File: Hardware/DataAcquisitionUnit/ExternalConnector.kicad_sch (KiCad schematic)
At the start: 3 parts, among them J1 DE9_Pins_MountingHoles, J2 Conn_Coaxial, J3 Conn_Coaxial

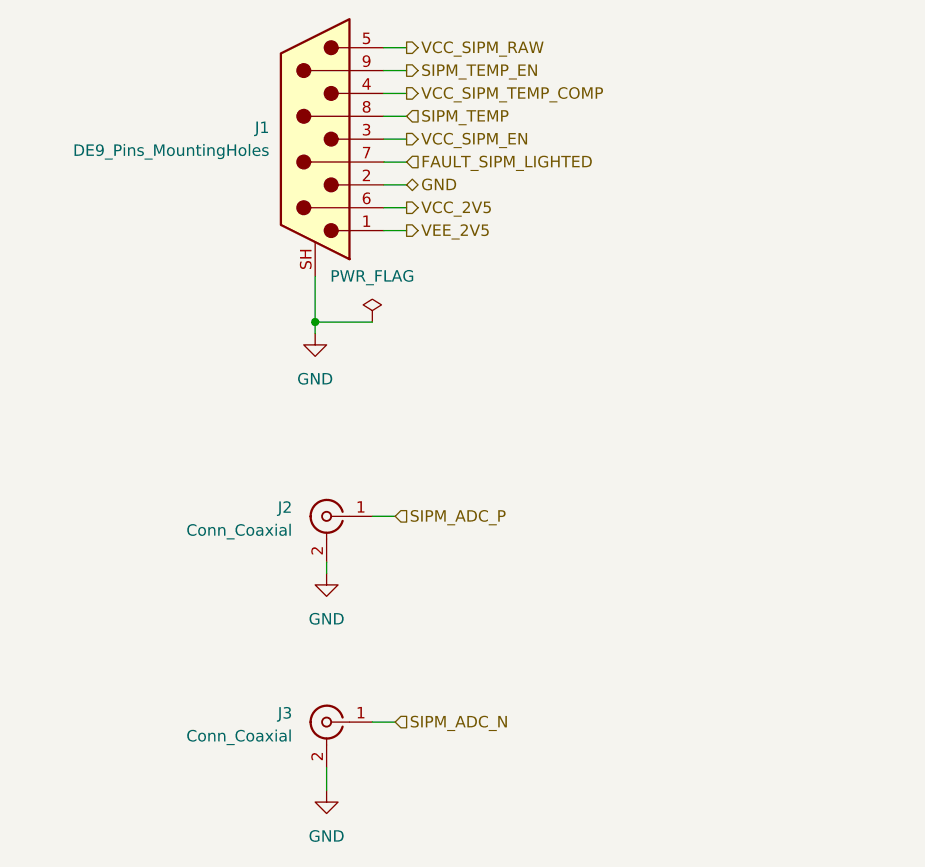
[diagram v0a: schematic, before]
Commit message: fix: #129, fix: #127
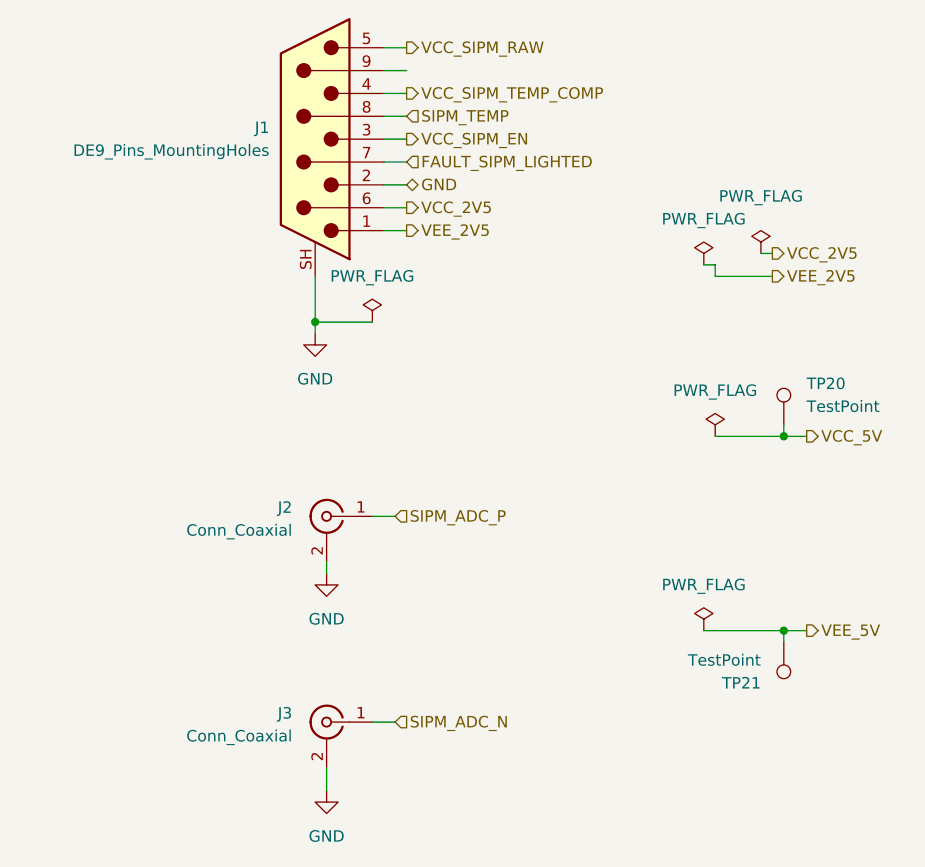
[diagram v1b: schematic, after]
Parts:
- added TP20, TP21: TestPoint, TestPoint:TestPoint_Pad_D1.5mm, symbol Connector:TestPoint
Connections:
- net SIPM_TEMP_EN: no longer names the net of J1.9
- new net VCC_5V: TP20.1
- new net VEE_5V: TP21.1
